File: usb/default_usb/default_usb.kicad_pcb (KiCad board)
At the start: 2 copper layers, 4 parts

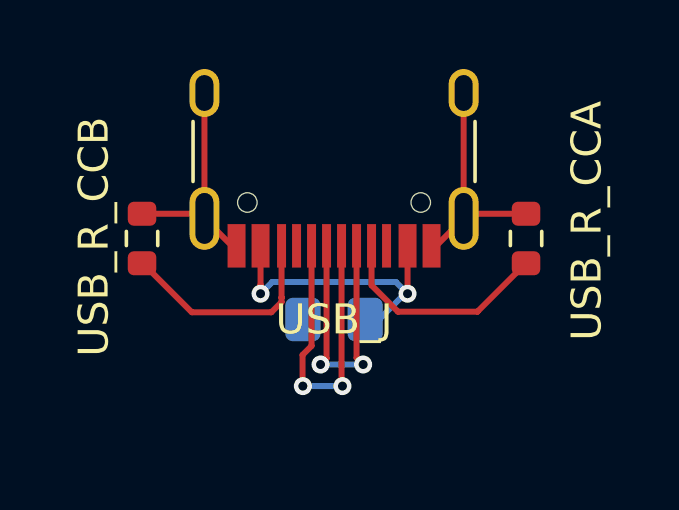
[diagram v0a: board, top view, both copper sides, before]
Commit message: update usb_c template
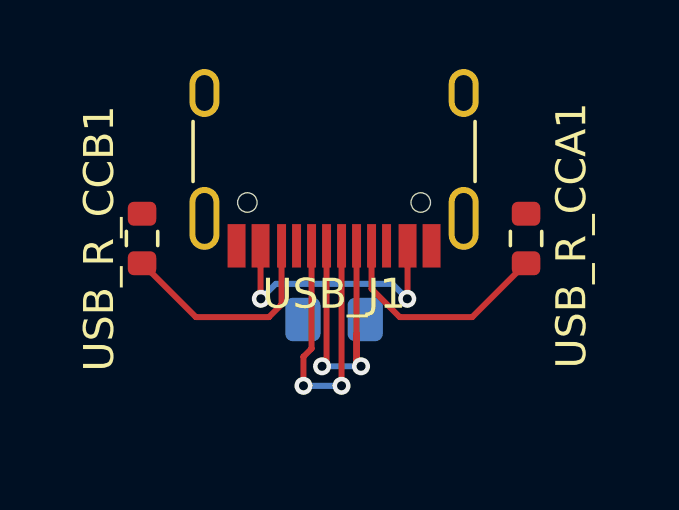
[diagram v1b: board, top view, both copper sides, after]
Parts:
- removed USB_C: 10nF, Capacitor_SMD:C_0805_2012Metric_Pad1.18x1.45mm_HandSolder
- removed USB_J: USB_C_Receptacle_USB2.0_16P, ErgoCai.pretty:USB_C_Receptacle_HRO_TYPE-C-31-M-12
- removed USB_R_CCA, USB_R_CCB: 5.1k, ErgoCai.pretty:R_0603_1608Metric
- added USB_C1: 10nF, ErgoCai.pretty:C_0805_2012Metric_Pad1.18x1.45mm_HandSolder, B.Cu at (0.00, 5.94)
- added USB_J1: USB_C_Receptacle_USB2.0_16P, ErgoCai.pretty:USB_C_Receptacle_HRO_TYPE-C-31-M-12, F.Cu at (0.00, -0.56)
- added USB_R_CCA1: 5.1k, ErgoCai.pretty:R_0603_1608Metric, F.Cu at (6.40, 3.24)
- added USB_R_CCB1: 5.1k, ErgoCai.pretty:R_0603_1608Metric, F.Cu at (-6.40, 3.24)
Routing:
- net GND: track 15.5 -> 0.00 mm
- net VBUS: track 10.3 -> 8.78 mm
- net DATA-: track 9.50 -> 10.8 mm

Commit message: remove old yaml template and update default usb pcb
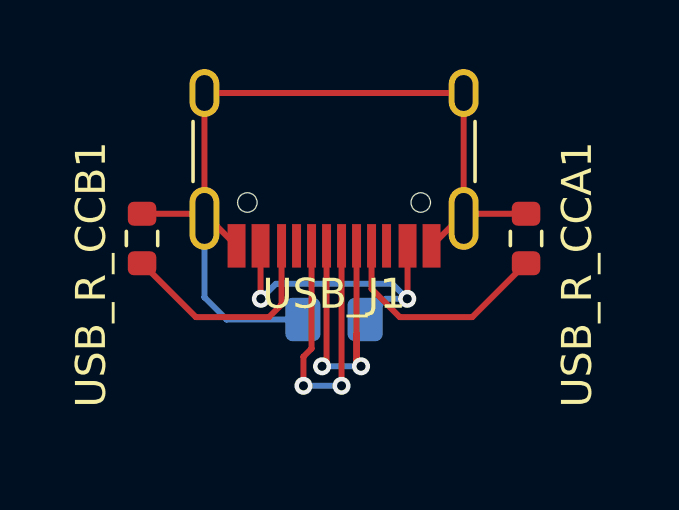
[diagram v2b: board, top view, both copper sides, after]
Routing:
- net GND: track 0.00 -> 30.4 mm
- net VBUS: track 8.78 -> 10.5 mm
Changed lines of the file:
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@@
 		(tags "resistor")
 		(property "Reference" "USB_R_CCB1"
-			(at 0 -1.43 90)
+			(at -1.2 -1.7 90)
 			(layer "F.SilkS")
 			(effects
@@
 		)
 		(property "Value" "5.1k"
-			(at -2.97 0.15 90)
+			(at -3 0 90)
 			(layer "F.Fab")
 			(effects
@@
 		(tags "resistor")
 		(property "Reference" "USB_R_CCA1"
-			(at 0.1 1.51 90)
+			(at -1.2 1.7 90)
 			(layer "F.SilkS")
 			(effects
@@
 		)
 		(property "Value" "5.1k"
-			(at -3.01 0.02 90)
+			(at -3 0 90)
 			(layer "F.Fab")
 			(effects
@@
 	)
 	(segment
+		(start 1.7275 5.25)
+		(end 1.0375 5.94)
+		(width 0.2)
+		(layer "B.Cu")
+		(net 1)
+	)
+	(segment
 		(start -1.94 4.75)
 		(end 1.94 4.75)
@@
 	)
 	(segment
+		(start 2.44 5.25)
+		(end 1.7275 5.25)
+		(width 0.2)
+		(layer "B.Cu")
+		(net 1)
+	)
+	(segment
 		(start 1.94 4.75)
 		(end 2.44 5.25)
@@
 	)
 	(segment
+		(start -4.165 2.57)
+		(end -3.25 3.485)
+		(width 0.2)
+		(layer "F.Cu")
+		(net 2)
+	)
+	(segment
+		(start -4.32 2.57)
+		(end -4.165 2.57)
+		(width 0.2)
+		(layer "F.Cu")
+		(net 2)
+	)
+	(segment
+		(start 4.32 2.57)
+		(end 4.165 2.57)
+		(width 0.2)
+		(layer "F.Cu")
+		(net 2)
+	)
+	(segment
+		(start 4.32 2.57)
+		(end 4.5 2.57)
+		(width 0.2)
+		(layer "F.Cu")
+		(net 2)
+	)
+	(segment
+		(start -4.32 -1.61)
+		(end 4.32 -1.61)
+		(width 0.2)
+		(layer "F.Cu")
+		(net 2)
+	)
+	(segment
+		(start -4.475 2.415)
+		(end -4.32 2.57)
+		(width 0.2)
+		(layer "F.Cu")
+		(net 2)
+	)
+	(segment
+		(start 4.5 2.57)
+		(end 4.655 2.415)
+		(width 0.2)
+		(layer "F.Cu")
+		(net 2)
+	)
+	(segment
+		(start 4.32 2.57)
+		(end 4.32 -1.61)
+		(width 0.2)
+		(layer "F.Cu")
+		(net 2)
+	)
+	(segment
+		(start 4.165 2.57)
+		(end 3.25 3.485)
+		(width 0.2)
+		(layer "F.Cu")
+		(net 2)
+	)
+	(segment
+		(start -4.32 -1.61)
+		(end -4.32 2.57)
+		(width 0.2)
+		(layer "F.Cu")
+		(net 2)
+	)
+	(segment
+		(start -6.4 2.415)
+		(end -4.475 2.415)
+		(width 0.2)
+		(layer "F.Cu")
+		(net 2)
+	)
+	(segment
+		(start 4.655 2.415)
+		(end 6.4 2.415)
+		(width 0.2)
+		(layer "F.Cu")
+		(net 2)
+	)
+	(segment
+		(start -1.0375 5.94)
+		(end -3.58 5.94)
+		(width 0.2)
+		(layer "B.Cu")
+		(net 2)
+	)
+	(segment
+		(start -3.58 5.94)
+		(end -4.32 5.2)
+		(width 0.2)
+		(layer "B.Cu")
+		(net 2)
+	)
+	(segment
+		(start -4.32 5.2)
+		(end -4.32 2.57)
+		(width 0.2)
+		(layer "B.Cu")
+		(net 2)
+	)
+	(segment

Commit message: move capacity to usb back
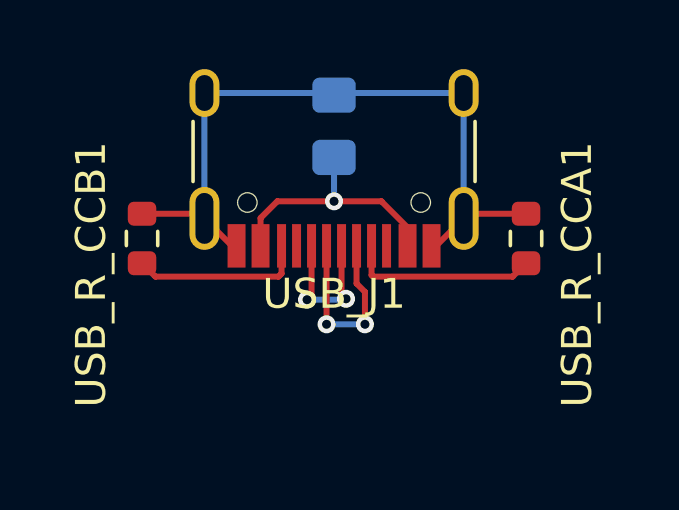
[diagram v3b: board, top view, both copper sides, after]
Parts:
- moved USB_C1 6.44 mm to (0.00, -0.50), turned to -90 degrees
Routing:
- net GND: track 30.4 -> 24.2 mm
- net DATA+: track 10.9 -> 5.00 mm
- net DATA-: track 10.8 -> 6.63 mm
- net VBUS: track 10.5 -> 8.49 mm, vias 2 -> 1
- net /CCB: track 7.52 -> 5.80 mm
- net /CCA: track 7.72 -> 6.33 mm

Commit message: correct usb pos
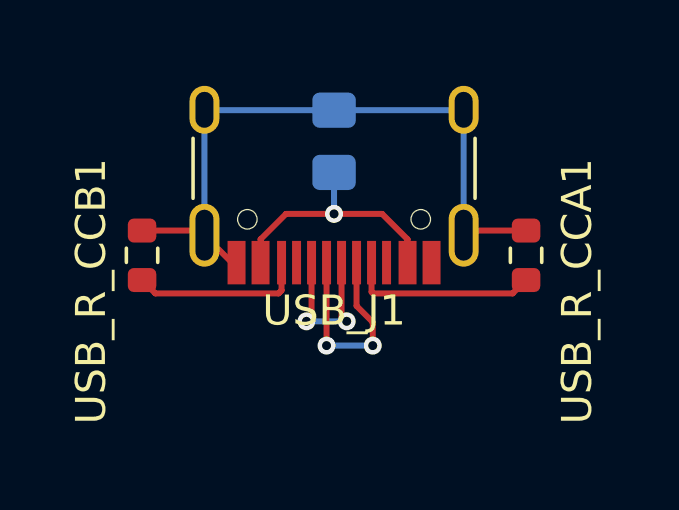
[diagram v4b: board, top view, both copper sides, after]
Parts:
- moved USB_J1 0.56 mm to (0.00, 0.00)
- moved USB_R_CCA1 0.56 mm to (6.40, 3.80)
- moved USB_R_CCB1 0.56 mm to (-6.40, 3.80)
- moved USB_C1 0.50 mm to (0.00, 0.00)
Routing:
- net GND: track 24.2 -> 22.7 mm
- net DATA-: track 6.63 -> 7.30 mm
- net DATA+: track 5.00 -> 5.50 mm
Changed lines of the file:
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@@
 	(footprint "ErgoCai.pretty:USB_C_Receptacle_HRO_TYPE-C-31-M-12"
 		(layer "F.Cu")
-		(at 0 -0.56 180)
+		(at 0 0 180)
 		(descr "USB Type-C receptacle for USB 2.0 and PD, http://www.krhro.com/uploads/soft/180320/1-1P320120243.pdf")
 		(tags "usb usb-c 2.0 pd")
@@
 	(footprint "ErgoCai.pretty:R_0603_1608Metric"
 		(layer "F.Cu")
-		(at -6.4 3.24 90)
+		(at -6.4 3.8 90)
 		(descr "Resistor SMD 0603 (1608 Metric), square (rectangular) end terminal, IPC_7351 nominal, (Body size source: IPC-SM-782 page 72, https://www.pcb-3d.com/wordpress/wp-content/uploads/ipc-sm-782a_amendment_1_and_2.pdf), generated with kicad-footprint-generator")
 		(tags "resistor")
@@
 	(footprint "ErgoCai.pretty:R_0603_1608Metric"
 		(layer "F.Cu")
-		(at 6.4 3.24 90)
+		(at 6.4 3.8 90)
 		(descr "Resistor SMD 0603 (1608 Metric), square (rectangular) end terminal, IPC_7351 nominal, (Body size source: IPC-SM-782 page 72, https://www.pcb-3d.com/wordpress/wp-content/uploads/ipc-sm-782a_amendment_1_and_2.pdf), generated with kicad-footprint-generator")
 		(tags "resistor")
@@
 	(footprint "ErgoCai.pretty:C_0805_2012Metric_Pad1.18x1.45mm_HandSolder"
 		(layer "B.Cu")
-		(at 0 -0.5 -90)
+		(at 0 0 -90)
 		(descr "Capacitor SMD 0805 (2012 Metric), square (rectangular) end terminal, IPC_7351 nominal with elongated pad for handsoldering. (Body size source: IPC-SM-782 page 76, https://www.pcb-3d.com/wordpress/wp-content/uploads/ipc-sm-782a_amendment_1_and_2.pdf, https://docs.google.com/spreadsheets/d/1BsfQQcO9C6DZCsRaXUlFlo91Tg2WpOkGARC1WS5S8t0/edit?usp=sharing), generated with kicad-footprint-generator")
 		(tags "capacitor handsolder")
 		(property "Reference" "USB_C1"
-			(at -2.61 0 180)
+			(at -2.61 0 0)
 			(layer "B.SilkS")
 			(effects
@@
 		)
 		(property "Value" "10nF"
-			(at 2.29 0.03 180)
+			(at 2.29 0.03 0)
 			(layer "B.Fab")
 			(effects
@@
 	)
 	(segment
-		(start -2.45 2.56)
-		(end -2.45 3.485)
+		(start -2.45 4.045)
+		(end -2.45 3.268)
 		(width 0.2)
 		(layer "F.Cu")
@@
 	)
 	(segment
-		(start -1.89 2)
-		(end -2.45 2.56)
+		(start -1.602 2.42)
+		(end 0 2.42)
 		(width 0.2)
 		(layer "F.Cu")
@@
 	)
 	(segment
-		(start 2.45 2.87)
-		(end 1.58 2)
+		(start 1.602 2.42)
+		(end 2.45 3.268)
 		(width 0.2)
 		(layer "F.Cu")
@@
 	)
 	(segment
-		(start 2.45 3.485)
-		(end 2.45 2.87)
+		(start 2.45 3.268)
+		(end 2.45 4.045)
 		(width 0.2)
 		(layer "F.Cu")
@@
 	)
 	(segment
-		(start 0 2)
-		(end -1.89 2)
+		(start -2.45 3.268)
+		(end -1.602 2.42)
 		(width 0.2)
 		(layer "F.Cu")
@@
 	)
 	(segment
-		(start 1.58 2)
-		(end 0 2)
+		(start 0 2.42)
+		(end 1.602 2.42)
 		(width 0.2)
 		(layer "F.Cu")
@@
 	)
 	(via
-		(at 0 2)
+		(at 0 2.42)
 		(size 0.6)
 		(drill 0.3)
@@
 	)
 	(segment
-		(start 0 0.5375)
-		(end 0 2)
+		(start 0 1.0375)
+		(end 0 2.42)
 		(width 0.2)
 		(layer "B.Cu")
@@
 	)
 	(segment
-		(start 4.475 2.415)
-		(end 4.32 2.57)
+		(start -6.4 2.975)
+		(end -4.475 2.975)
 		(width 0.2)
 		(layer "F.Cu")
@@
 	)
 	(segment
-		(start 3.25 3.485)
-		(end 3.405 3.485)
+		(start -3.25 4.045)
+		(end -3.405 4.045)
 		(width 0.2)
 		(layer "F.Cu")
@@
 	)
 	(segment
-		(start -4.475 2.415)
-		(end -4.32 2.57)
+		(start 6.4 2.975)
+		(end 4.475 2.975)
 		(width 0.2)
 		(layer "F.Cu")
@@
 	)
 	(segment
-		(start 3.405 3.485)
-		(end 4.32 2.57)
+		(start -3.405 4.045)
+		(end -4.32 3.13)
 		(width 0.2)
 		(layer "F.Cu")
@@
 	)
 	(segment
-		(start -3.25 3.485)
-		(end -3.405 3.485)
+		(start -4.475 2.975)
+		(end -4.32 3.13)
 		(width 0.2)
 		(layer "F.Cu")
@@
 	)
 	(segment
-		(start -3.405 3.485)
-		(end -4.32 2.57)
+		(start 4.475 2.975)
+		(end 4.32 3.13)
 		(width 0.2)
 		(layer "F.Cu")
@@
 	)
 	(segment
-		(start -6.4 2.415)
-		(end -4.475 2.415)
-		(width 0.2)
-		(layer "F.Cu")
-		(net 2)
-	)
-	(segment
-		(start 6.4 2.415)
-		(end 4.475 2.415)
-		(width 0.2)
-		(layer "F.Cu")
-		(net 2)
-	)
-	(segment
-		(start -4.32 2.57)
-		(end -4.32 -1.61)
+		(start 4.3075 -1.0375)
+		(end 4.32 -1.05)
 		(width 0.2)
 		(layer "B.Cu")
@@
 	)
 	(segment
-		(start 0.12 -1.61)
-		(end 4.32 -1.61)
+		(start 4.32 -1.05)
+		(end 4.32 3.13)
 		(width 0.2)
 		(layer "B.Cu")
@@
 	)
 	(segment
-		(start -4.32 -1.61)
-		(end -0.0725 -1.61)
+		(start 0 -1.0375)
+		(end -4.3075 -1.0375)
 		(width 0.2)
 		(layer "B.Cu")
@@
 	)
 	(segment
-		(start 0 -1.5375)
-		(end 0.0475 -1.5375)
+		(start 0 -1.0375)
+		(end 4.3075 -1.0375)
 		(width 0.2)
 		(layer "B.Cu")
@@
 	)
 	(segment
-		(start 0.0475 -1.5375)
-		(end 0.12 -1.61)
+		(start -4.32 -1.05)
+		(end -4.32 3.13)
 		(width 0.2)
 		(layer "B.Cu")
@@
 	)
 	(segment
-		(start -0.0725 -1.61)
-		(end 0 -1.5375)
+		(start -4.3075 -1.0375)
+		(end -4.32 -1.05)
 		(width 0.2)
 		(layer "B.Cu")
@@
 	)
 	(segment
-		(start 4.32 -1.61)
-		(end 4.32 2.57)
-		(width 0.2)
-		(layer "B.Cu")
-		(net 2)
-	)
-	(segment
-		(start 1.03 5.02)
-		(end 1.03 6.1)
+		(start 1.29 6.05)
+		(end 1.29 6.81)
 		(width 0.2)
 		(layer "F.Cu")
@@
 	)
 	(segment
-		(start 0.75 3.485)
-		(end 0.75 4.74)
+		(start 1.3 6.04)
+		(end 1.29 6.05)
 		(width 0.2)
 		(layer "F.Cu")
@@
 	)
 	(segment
-		(start 0.75 4.74)
-		(end 1.03 5.02)
+		(start 0.75 5.49)
+		(end 1.3 6.04)
 		(width 0.2)
 		(layer "F.Cu")
@@
 	)
 	(segment
-		(start -0.25 3.485)
-		(end -0.25 6.1)
+		(start 0.75 4.045)
+		(end 0.75 5.49)
 		(width 0.2)
 		(layer "F.Cu")
 		(net 3)
 	)
+	(segment
+		(start -0.25 4.045)
+		(end -0.25 6.81)
+		(width 0.2)
+		(layer "F.Cu")
+		(net 3)
+	)
 	(via
-		(at 1.03 6.1)
+		(at 1.29 6.81)
 		(size 0.6)
 		(drill 0.3)
@@
 	)
 	(via
-		(at -0.25 6.1)
+		(at -0.25 6.81)
 		(size 0.6)
 		(drill 0.3)
@@
 	)
 	(segment
-		(start -0.25 6.1)
-		(end 1.03 6.1)
+		(start -0.25 6.81)
+		(end 1.29 6.81)
 		(width 0.2)
 		(layer "B.Cu")
@@
 	)
 	(segment
-		(start 5.954 4.511)
-		(end 6.4 4.065)
+		(start 5.954 5.071)
+		(end 1.299 5.071)
 		(width 0.2)
 		(layer "F.Cu")
@@
 	)
 	(segment
-		(start 1.25 3.485)
-		(end 1.25 4.462)
+		(start 1.25 5.022)
+		(end 1.25 4.045)
 		(width 0.2)
 		(layer "F.Cu")
@@
 	)
 	(segment
-		(start 1.299 4.511)
-		(end 5.954 4.511)
+		(start 1.299 5.071)
+		(end 1.25 5.022)
 		(width 0.2)
 		(layer "F.Cu")
@@
 	)
 	(segment
-		(start 1.25 4.462)
-		(end 1.299 4.511)
+		(start 6.4 4.625)
+		(end 5.954 5.071)
 		(width 0.2)
 		(layer "F.Cu")
@@
 	)
 	(segment
-		(start -0.9 5.28)
-		(end -0.75 5.13)
+		(start 0.25 5.852959)
+		(end 0.422054 6.025013)
 		(width 0.2)
 		(layer "F.Cu")
@@
 	)
 	(segment
-		(start -0.75 5.13)
-		(end -0.75 3.485)
+		(start -0.75 5.91)
+		(end -0.92 6.08)
 		(width 0.2)
 		(layer "F.Cu")
@@
 	)
 	(segment
-		(start 0.25 5.1)
-		(end 0.4 5.25)
+		(start -0.75 4.045)
+		(end -0.75 5.91)
 		(width 0.2)
 		(layer "F.Cu")
@@
 	)
 	(segment
-		(start 0.25 3.485)
-		(end 0.25 5.1)
+		(start 0.25 4.045)
+		(end 0.25 5.852959)
 		(width 0.2)
 		(layer "F.Cu")
@@
 	)
 	(via
-		(at 0.4 5.25)
+		(at -0.92 6)
 		(size 0.6)
 		(drill 0.3)
@@
 	)
 	(via
-		(at -0.9 5.28)
+		(at 0.422054 6)
 		(size 0.6)
 		(drill 0.3)
@@
 	)
 	(segment
-		(start -0.9 5.28)
-		(end 0.37 5.28)
+		(start -0.92 6)
+		(end 0.422054 6)
 		(width 0.2)
 		(layer "B.Cu")
@@
 	)
 	(segment
-		(start 0.37 5.28)
-		(end 0.4 5.25)
-		(width 0.2)
-		(layer "B.Cu")
-		(net 5)
-	)
-	(segment
-		(start -1.75 4.412)
-		(end -1.849 4.511)
+		(start -5.954 5.071)
+		(end -6.4 4.625)
 		(width 0.2)
 		(layer "F.Cu")
@@
 	)
 	(segment
-		(start -1.75 3.485)
-		(end -1.75 4.412)
+		(start -1.75 4.045)
+		(end -1.75 4.972)
 		(width 0.2)
 		(layer "F.Cu")
@@
 	)
 	(segment
-		(start -1.849 4.511)
-		(end -5.954 4.511)
+		(start -1.849 5.071)
+		(end -5.954 5.071)
 		(width 0.2)
 		(layer "F.Cu")
@@
 	)
 	(segment
-		(start -5.954 4.511)
-		(end -6.4 4.065)
-		(width 0.2)
-		(layer "F.Cu")
+		(start -1.75 4.972)
+		(end -1.849 5.071)
+		(width 0.2)
+		(layer "F.Cu")

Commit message: correct usb pos
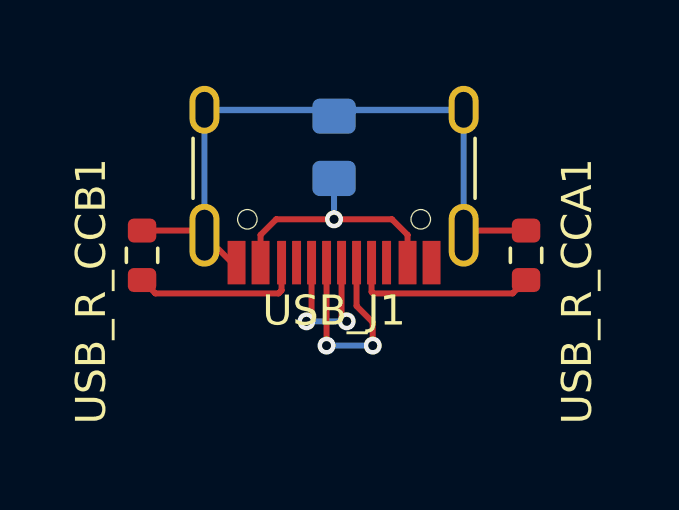
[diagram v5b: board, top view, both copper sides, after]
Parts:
- moved USB_C1 0.20 mm to (0.00, 0.20)
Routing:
- net GND: track 22.7 -> 31.6 mm
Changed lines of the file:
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@@
 	(footprint "ErgoCai.pretty:C_0805_2012Metric_Pad1.18x1.45mm_HandSolder"
 		(layer "B.Cu")
-		(at 0 0 -90)
+		(at 0 0.2 -90)
 		(descr "Capacitor SMD 0805 (2012 Metric), square (rectangular) end terminal, IPC_7351 nominal with elongated pad for handsoldering. (Body size source: IPC-SM-782 page 76, https://www.pcb-3d.com/wordpress/wp-content/uploads/ipc-sm-782a_amendment_1_and_2.pdf, https://docs.google.com/spreadsheets/d/1BsfQQcO9C6DZCsRaXUlFlo91Tg2WpOkGARC1WS5S8t0/edit?usp=sharing), generated with kicad-footprint-generator")
 		(tags "capacitor handsolder")
@@
 	)
 	(segment
+		(start -1.93 2.6)
+		(end -0.01 2.6)
+		(width 0.2)
+		(layer "F.Cu")
+		(net 1)
+	)
+	(segment
+		(start 2.45 3.12)
+		(end 1.93 2.6)
+		(width 0.2)
+		(layer "F.Cu")
+		(net 1)
+	)
+	(segment
 		(start -2.45 4.045)
-		(end -2.45 3.268)
-		(width 0.2)
-		(layer "F.Cu")
-		(net 1)
-	)
-	(segment
-		(start -1.602 2.42)
-		(end 0 2.42)
-		(width 0.2)
-		(layer "F.Cu")
-		(net 1)
-	)
-	(segment
-		(start 1.602 2.42)
-		(end 2.45 3.268)
-		(width 0.2)
-		(layer "F.Cu")
-		(net 1)
-	)
-	(segment
-		(start 2.45 3.268)
-		(end 2.45 4.045)
-		(width 0.2)
-		(layer "F.Cu")
-		(net 1)
-	)
-	(segment
-		(start -2.45 3.268)
-		(end -1.602 2.42)
-		(width 0.2)
-		(layer "F.Cu")
-		(net 1)
-	)
-	(segment
-		(start 0 2.42)
-		(end 1.602 2.42)
+		(end -2.45 3.12)
+		(width 0.2)
+		(layer "F.Cu")
+		(net 1)
+	)
+	(segment
+		(start -2.45 3.12)
+		(end -1.93 2.6)
+		(width 0.2)
+		(layer "F.Cu")
+		(net 1)
+	)
+	(segment
+		(start 1.93 2.6)
+		(end -0.01 2.6)
+		(width 0.2)
+		(layer "F.Cu")
+		(net 1)
+	)
+	(segment
+		(start 2.45 4.045)
+		(end 2.45 3.12)
 		(width 0.2)
 		(layer "F.Cu")
@@
 	)
 	(via
-		(at 0 2.42)
+		(at 0 2.6)
 		(size 0.6)
 		(drill 0.3)
@@
 	)
 	(segment
-		(start 0 1.0375)
-		(end 0 2.42)
+		(start 0 1.2375)
+		(end 0 2.6)
+		(width 0.2)
+		(layer "B.Cu")
+		(net 1)
+	)
+	(segment
+		(start 0 2.59)
+		(end -0.01 2.6)
 		(width 0.2)
 		(layer "B.Cu")
@@
 	)
 	(segment
+		(start 0.2125 -1.05)
+		(end 0 -0.8375)
+		(width 0.2)
+		(layer "B.Cu")
+		(net 2)
+	)
+	(segment
 		(start 4.3075 -1.0375)
 		(end 4.32 -1.05)
@@
 	)
 	(segment
+		(start -0.2125 -1.05)
+		(end 0 -0.8375)
+		(width 0.2)
+		(layer "B.Cu")
+		(net 2)
+	)
+	(segment
 		(start -4.32 -1.05)
 		(end -4.32 3.13)
@@
 		(width 0.2)
 		(layer "B.Cu")
+		(net 2)
+	)
+	(segment
+		(start -4.32 -1.05)
+		(end -0.2125 -1.05)
+		(width 0.2)
+		(layer "B.Cu")
+		(net 2)
+	)
+	(segment
+		(start 4.32 -1.05)
+		(end 0.2125 -1.05)
+		(width 0.2)
+		(layer "B.Cu")

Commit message: add usb gnd connection
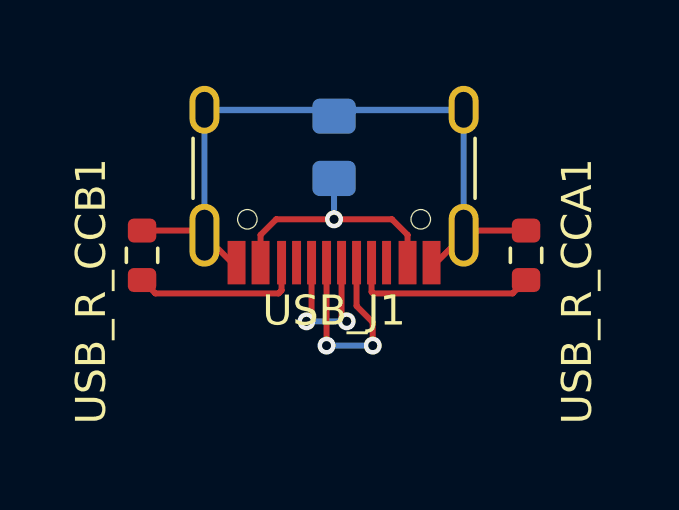
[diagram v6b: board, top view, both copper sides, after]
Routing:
- net GND: track 31.6 -> 33.0 mm
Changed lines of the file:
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@@
+	)
+	(segment
+		(start 3.25 4.045)
+		(end 3.405 4.045)
+		(width 0.2)
+		(layer "F.Cu")
+		(net 2)
 	)
 	(segment
@@
 		(end 4.32 3.13)
 		(width 0.2)
+		(layer "F.Cu")
+		(net 2)
+	)
+	(segment
+		(start 3.405 4.045)
+		(end 4.32 3.13)
+		(width 0.2)

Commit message: update vbus route
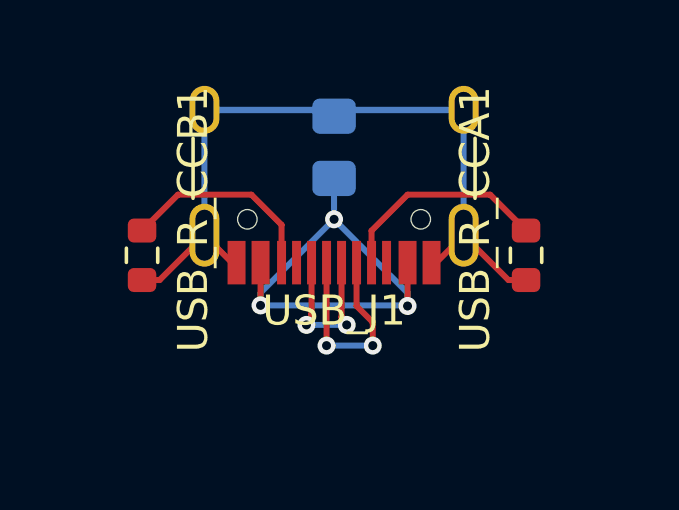
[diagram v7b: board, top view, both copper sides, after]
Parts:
- turned USB_R_CCA1 to -90 degrees
- turned USB_R_CCB1 to -90 degrees
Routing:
- net VBUS: track 8.56 -> 16.9 mm, vias 1 -> 3
- net GND: track 33.0 -> 34.6 mm
- net /CCB: track 5.80 -> 6.82 mm
- net /CCA: track 6.33 -> 7.21 mm
- net DATA+: track 5.50 -> 6.28 mm
